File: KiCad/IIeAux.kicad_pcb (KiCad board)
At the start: 4 copper layers, 88.9 x 77.5 mm, 21 parts, among them J1 Apple IIe Aux, J4 PAL, U1 SN74LVC245AN, U2 TangNano9K, U3 74LS245, U4 74LS374, U5 SN74LVC245AN, U6 SN74LVC245AN, U7 SN74LVC245AN, U8 AE-LCNV4-MOSFET

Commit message: PCB V1.1
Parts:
- removed J4: PAL, IIeAux:PinHeader_1x02_P2.54mm_Horizontal
- removed R2: 0, IIeAux:R_Axial_DIN0207_L6.3mm_D2.5mm_P10.16mm_Horizontal
- removed the U8 at (109.9, 107.3)
- added C6: 0.1u, IIeAux:C_Disc_D4.3mm_W1.9mm_P5.08mm, F.Cu at (169.5, 111.8)
- added J2: Double Hi-Res, IIeAux:PinHeader_1x02_P2.54mm_Horizontal, F.Cu at (117.5, 131.4)
- added J3: PAL, IIeAux:PinHeader_1x02_P2.54mm_Horizontal, F.Cu at (118.1, 83.2)
- added U2: SN74LVC245AN, IIeAux:DIP-20_W7.62mm_Socket, F.Cu at (114.3, 105.4)
- J1: value Apple IIe Aux -> Aux Slot
- R1: value 4K7 -> R
- U3: renamed from U5; footprint IIeAux:DIP-20_W7.62mm -> IIeAux:DIP-20_W7.62mm_Socket
- U4: renamed from U6; footprint IIeAux:DIP-20_W7.62mm -> IIeAux:DIP-20_W7.62mm_Socket
- U5: renamed from U1; footprint IIeAux:DIP-20_W7.62mm -> IIeAux:DIP-20_W7.62mm_Socket
- U8: renamed from U7; footprint IIeAux:DIP-20_W7.62mm -> IIeAux:DIP-20_W7.62mm_Socket
- moved C7 62.7 mm to (169.5, 123.2)
- moved U7 46.7 mm to (172.7, 119.4)
- moved RN1 43.2 mm to (172.7, 108.6)
- moved C4 43.2 mm to (111.1, 111.8)
- moved U3 27.7 mm to (143.5, 105.4)
- moved U4 27.7 mm to (172.7, 105.4)
- moved C3 27.7 mm to (169.5, 97.8)
- moved C2 27.4 mm to (140.3, 97.8)
- moved U8 19.8 mm to (172.7, 130.8)
- moved C5 19.1 mm to (140.3, 111.8)
- moved C1 18.0 mm to (111.1, 97.8)
- moved U6 16.9 mm to (143.5, 119.4)
- moved U1 16.9 mm to (135.9, 94.6)
- moved D1 13.9 mm to (198.1, 71.8)
- moved U5 12.8 mm to (114.3, 119.4)
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- renumbered C5 to C2, C2 to C4, C6 to C5, C4 to C7, C7 to C8, U2 to U1, U4 to U6, U3 to U7
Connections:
- net Net-(U2-IOT10A_84) renamed A5
- net Net-(U2-IOT10B_83) renamed A4
- net Net-(U2-IOT11A_82) renamed A3
- net Net-(U2-IOT11B_81) renamed A2
- net Net-(U2-IOT12A_80) renamed A1
- net Net-(U2-IOT12B_79) renamed A0
- net Net-(U2-IOT8A_86) renamed A7
- net Net-(U2-IOT8B_85) renamed A6
- C2 pad 1: +5V -> +3V3
- U1 pad 1: Net-(U2-38_IOB31B) -> RA_EN
- U1 pad 10: Net-(U1-A6) -> Net-(U1-30_IOB13B)
- U1 pad 11: Net-(U1-A7) -> Net-(U1-33_IOB23A)
- U1 pad 12: Net-(U1-A8) -> Net-(U1-34_IOB23B)
- U1 pad 13: Net-(U2-40_IOB33B) -> Net-(U1-40_IOB33B)
- U1 pad 14: Net-(U2-35_IOB29A) -> Net-(U1-35_IOB29A)
- U1 pad 2: Net-(U2-37_IOB31A) -> VID_EN
- U1 pad 27: Net-(U2-IOB15B_32) -> Net-(U1-IOB15B_32)
- U1 pad 28: Net-(U2-IOB15A_31) -> Net-(U1-IOB15A_31)
- U1 pad 29: Net-(U2-IOR24A_49) -> Net-(U1-IOR24A_49)
- U1 pad 3: Net-(U2-36_IOB29B) -> D_R/W
- U1 pad 30: Net-(U2-IOR24B_48) -> Net-(U1-IOR24B_48)
- U1 pad 38: Net-(U2-IOT37B_76) -> Net-(U1-IOT37B_76)
- U1 pad 39: Net-(U2-IOT37A_77) -> Net-(U1-IOT37A_77)
- U1 pad 4: Net-(U2-39_IOB33A) -> MD_EN
- U1 pad 5: Net-(U1-A1) -> Net-(U1-25_IOB8A)
- U1 pad 6: Net-(U1-A2) -> Net-(U1-26_IOB8B)
- U1 pad 7: Net-(U1-A3) -> Net-(U1-27_IOB11A)
- U1 pad 8: Net-(U1-A4) -> Net-(U1-28_IOB11B)
- U1 pad 9: Net-(U1-A5) -> Net-(U1-29_IOB13A)
- U3 pad 19: GND -> VID_EN
- U3 pad 2: RA0 -> VID7
- U3 pad 3: RA1 -> VID6
- U3 pad 4: RA2 -> VID5
- U3 pad 5: RA3 -> VID4
- U3 pad 6: RA4 -> VID3
- U3 pad 7: RA5 -> VID2
- U3 pad 8: RA6 -> VID1
- U3 pad 9: RA7 -> VID0
- U4 pad 1: +3V3 -> D_R/W
- U4 pad 11: Net-(U2-35_IOB29A) -> Net-(U1-IOB15B_32)
- U4 pad 12: Net-(U2-40_IOB33B) -> Net-(U1-IOB15A_31)
- U4 pad 13: Net-(U2-IOB15B_32) -> Net-(U1-IOR24A_49)
- U4 pad 14: Net-(U2-IOB15A_31) -> Net-(U1-IOR24B_48)
- U4 pad 15: Net-(U2-IOR24A_49) -> Net-(U1-IOT37B_76)
- U4 pad 16: Net-(U2-IOR24B_48) -> Net-(U1-IOT37A_77)
- U4 pad 17: Net-(U2-IOT37B_76) -> Net-(U1-40_IOB33B)
- U4 pad 18: Net-(U2-IOT37A_77) -> Net-(U1-35_IOB29A)
- U4 pad 2: VID0 -> D0
- U4 pad 3: VID1 -> D1
- U4 pad 4: VID2 -> D2
- U4 pad 5: VID3 -> D3
- U4 pad 6: VID4 -> D4
- U4 pad 7: VID5 -> D5
- U4 pad 8: VID6 -> D6
- U4 pad 9: VID7 -> D7
- U5 pad 1: R/W80 -> +3V3
- U5 pad 11: D7 -> Net-(U1-34_IOB23B)
- U5 pad 12: D6 -> Net-(U1-33_IOB23A)
- U5 pad 13: D5 -> Net-(U1-30_IOB13B)
- U5 pad 14: D4 -> Net-(U1-29_IOB13A)
- U5 pad 15: D3 -> Net-(U1-28_IOB11B)
- U5 pad 16: D2 -> Net-(U1-27_IOB11A)
- U5 pad 17: D1 -> Net-(U1-26_IOB8B)
- U5 pad 18: D0 -> Net-(U1-25_IOB8A)
- U5 pad 2: Net-(U1-A1) -> GR
- U5 pad 3: Net-(U1-A2) -> RA10
- U5 pad 4: Net-(U1-A3) -> RA9
- U5 pad 5: Net-(U1-A4) -> Q3
- U5 pad 6: Net-(U1-A5) -> SYNC
- U5 pad 7: Net-(U1-A6) -> PRAS
- U5 pad 8: Net-(U1-A7) -> C07X
- U5 pad 9: Net-(U1-A8) -> R/W
- U6 pad 12: VID4 -> VID3
- U6 pad 13: D4 -> D3
- U6 pad 14: D5 -> D2
- U6 pad 15: VID5 -> VID2
- U6 pad 16: VID6 -> VID1
- U6 pad 17: D6 -> D1
- U6 pad 18: D7 -> D0
- U6 pad 19: VID7 -> VID0
- U6 pad 2: VID0 -> VID7
- U6 pad 3: D0 -> D7
- U6 pad 4: D1 -> D6
- U6 pad 5: VID1 -> VID6
- U6 pad 6: VID2 -> VID5
- U6 pad 7: D2 -> D5
- U6 pad 8: D3 -> D4
- U6 pad 9: VID3 -> VID4
- U7 pad 19: EN80 -> MD_EN
- U8 pad 2: PRAS -> PHI0
- U8 pad 3: Q3 -> PHI1
- U8 pad 4: R/W80 -> 80VID
- U8 pad 5: GR -> EN80
- U8 pad 6: 80VID -> R/W80
- U8 pad 7: AN3 -> LDPS
- U8 pad 8: SYNC -> 14M
- U8 pad 9: 14M -> AN3
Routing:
- net AN3: track 46.9 -> 229.5 mm, vias 1 -> 0
- net +5V: track 249.5 -> 153.7 mm, vias 0 -> 3
- net EN80: track 102.5 -> 11.4 mm, vias 2 -> 0
- net Net-(U1-41_IOB41A): track 7.92 -> 95.9 mm
- net D0: track 127.4 -> 43.8 mm, vias 2 -> 0
- net VID7: track 127.9 -> 44.7 mm, vias 1 -> 0
- net RA6: track 134.2 -> 52.3 mm, vias 1 -> 0
- net R/W80: track 93.7 -> 12.3 mm, vias 2 -> 0
- net D2: track 118.5 -> 37.4 mm, vias 2 -> 0
- net RA7: track 121.6 -> 41.7 mm, vias 2 -> 1
- net Net-(U1-42_IOB41B): track 7.92 -> 87.7 mm
- net D1: track 122.7 -> 43.8 mm, vias 2 -> 0
- net RA5: track 131.1 -> 55.2 mm, vias 0 -> 1
- net D3: track 112.5 -> 37.4 mm, vias 2 -> 0
- net +3V3: track 237.4 -> 309.9 mm
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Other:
- board size 88.9 x 77.5 mm -> 99.7 x 77.5 mm
- board text added: "IIeAux RGB Card"
- board text added: "V1.1 2026 nanja.info"
- board text removed: "2026 nanja.info"

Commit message: V1.0 first batch
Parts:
- removed the C6 at (169.5, 111.8)
- removed the U2 at (114.3, 105.4)
- added J4: PAL, IIeAux:PinHeader_1x02_P2.54mm_Horizontal, F.Cu at (118.1, 85.1)
- added J5: Y, IIeAux:PinSocket_1x08_P2.54mm_Vertical, B.Cu at (160.0, 117.5)
- added J6: X, IIeAux:PinSocket_1x08_P2.54mm_Vertical, B.Cu at (166.4, 76.2)
- J1: value Aux Slot -> Apple IIe Aux
- J2: value Double Hi-Res -> Double HiRes
- J3: value PAL -> Aux; footprint IIeAux:PinHeader_1x02_P2.54mm_Horizontal -> IIeAux:PinSocket_2x30_P2.54mm; moved to B.Cu
- R1: value R -> 4K7
- U1: renamed from U5; footprint IIeAux:DIP-20_W7.62mm_Socket -> IIeAux:DIP-20_W7.62mm
- U5: renamed from U3; footprint IIeAux:DIP-20_W7.62mm_Socket -> IIeAux:DIP-20_W7.62mm
- U6: renamed from U4; footprint IIeAux:DIP-20_W7.62mm_Socket -> IIeAux:DIP-20_W7.62mm
- U7: renamed from U8; footprint IIeAux:DIP-20_W7.62mm_Socket -> IIeAux:DIP-20_W7.62mm
- moved C2 73.1 mm to (184.2, 109.2)
- moved C4 58.5 mm to (131.4, 78.7), turned to 90 degrees
- moved J3 52.7 mm to (119.4, 135.9), turned to -90 degrees
- moved C5 50.0 mm to (184.2, 121.9)
- moved U3 46.8 mm to (127.0, 129.5)
- moved RN1 46.6 mm to (127.0, 117.5)
- moved D2 33.3 mm to (190.5, 104.1)
- moved C3 32.0 mm to (190.5, 73.7)
- moved U6 28.1 mm to (163.8, 78.7)
- moved U5 27.7 mm to (135.9, 78.7)
- moved U7 22.5 mm to (157.5, 114.3)
- moved C6 21.0 mm to (121.9, 121.9)
- moved C7 19.4 mm to (190.5, 120.7), turned to 0 degrees
- moved U4 17.3 mm to (157.5, 129.5)
- moved U2 16.9 mm to (121.9, 104.1)
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- renumbered C4 to C2, C7 to C4, C2 to C5, C5 to C6, C8 to C7, D1 to D2, U1 to U2, U7 to U3, U6 to U4
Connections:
- net A0 renamed Net-(U2-IOT12B_79)
- net A1 renamed Net-(U2-IOT12A_80)
- net A2 renamed Net-(U2-IOT11B_81)
- net A3 renamed Net-(U2-IOT11A_82)
- net A4 renamed Net-(U2-IOT10B_83)
- net A5 renamed Net-(U2-IOT10A_84)
- net A6 renamed Net-(U2-IOT8B_85)
- net A7 renamed Net-(U2-IOT8A_86)
- C5 pad 1: +3V3 -> +5V
- J3 pad 1: GND -> 3.58M
- J3 pad 2: Net-(J3-Pin_2) -> VID7M
- R1 pad 2: Net-(J3-Pin_2) -> Net-(J4-Pin_1)
- U1 pad 1: +3V3 -> R/W
- U1 pad 2: GR -> D0
- U1 pad 3: RA10 -> D1
- U1 pad 4: RA9 -> D2
- U1 pad 5: Q3 -> D3
- U1 pad 6: SYNC -> D4
- U1 pad 7: PRAS -> D5
- U1 pad 8: C07X -> D6
- U1 pad 9: R/W -> D7
- U2 pad 1: RA_EN -> unconnected-(U2-38_IOB31B-Pad1)
- U2 pad 13: Net-(U1-40_IOB33B) -> Net-(U2-40_IOB33B)
- U2 pad 14: Net-(U1-35_IOB29A) -> Net-(U2-35_IOB29A)
- U2 pad 2: VID_EN -> unconnected-(U2-37_IOB31A-Pad2)
- U2 pad 27: Net-(U1-IOB15B_32) -> Net-(U2-IOB15B_32)
- U2 pad 28: Net-(U1-IOB15A_31) -> Net-(U2-IOB15A_31)
- U2 pad 29: Net-(U1-IOR24A_49) -> Net-(U2-IOR24A_49)
- U2 pad 3: D_R/W -> unconnected-(U2-36_IOB29B-Pad3)
- U2 pad 30: Net-(U1-IOR24B_48) -> Net-(U2-IOR24B_48)
- U2 pad 38: Net-(U1-IOT37B_76) -> Net-(U2-IOT37B_76)
- U2 pad 39: Net-(U1-IOT37A_77) -> Net-(U2-IOT37A_77)
- U2 pad 4: MD_EN -> unconnected-(U2-39_IOB33A-Pad4)
- U2 pad 48: Net-(J3-Pin_2) -> Net-(J4-Pin_1)
- U3 pad 19: MD_EN -> EN80
- U4 pad 12: VID3 -> VID4
- U4 pad 13: D3 -> D4
- U4 pad 14: D2 -> D5
- U4 pad 15: VID2 -> VID5
- U4 pad 16: VID1 -> VID6
- U4 pad 17: D1 -> D6
- U4 pad 18: D0 -> D7
- U4 pad 19: VID0 -> VID7
- U4 pad 2: VID7 -> VID0
- U4 pad 3: D7 -> D0
- U4 pad 4: D6 -> D1
- U4 pad 5: VID6 -> VID1
- U4 pad 6: VID5 -> VID2
- U4 pad 7: D5 -> D2
- U4 pad 8: D4 -> D3
- U4 pad 9: VID4 -> VID3
- U5 pad 19: VID_EN -> GND
- U5 pad 2: VID7 -> RA0
- U5 pad 3: VID6 -> RA1
- U5 pad 4: VID5 -> RA2
- U5 pad 5: VID4 -> RA3
- U5 pad 6: VID3 -> RA4
- U5 pad 7: VID2 -> RA5
- U5 pad 8: VID1 -> RA6
- U5 pad 9: VID0 -> RA7
- U6 pad 1: D_R/W -> +3V3
- U6 pad 11: Net-(U1-IOB15B_32) -> Net-(U2-35_IOB29A)
- U6 pad 12: Net-(U1-IOB15A_31) -> Net-(U2-40_IOB33B)
- U6 pad 13: Net-(U1-IOR24A_49) -> Net-(U2-IOB15B_32)
- U6 pad 14: Net-(U1-IOR24B_48) -> Net-(U2-IOB15A_31)
- U6 pad 15: Net-(U1-IOT37B_76) -> Net-(U2-IOR24A_49)
- U6 pad 16: Net-(U1-IOT37A_77) -> Net-(U2-IOR24B_48)
- U6 pad 17: Net-(U1-40_IOB33B) -> Net-(U2-IOT37B_76)
- U6 pad 18: Net-(U1-35_IOB29A) -> Net-(U2-IOT37A_77)
- U6 pad 2: D0 -> X0
- U6 pad 3: D1 -> X1
- U6 pad 4: D2 -> X2
- U6 pad 5: D3 -> X3
- U6 pad 6: D4 -> X4
- U6 pad 7: D5 -> X5
- U6 pad 8: D6 -> X6
- U6 pad 9: D7 -> X7
- U7 pad 2: PHI0 -> Y0
- U7 pad 3: PHI1 -> Y1
- U7 pad 4: 80VID -> Y2
- U7 pad 5: EN80 -> Y3
- U7 pad 6: R/W80 -> Y4
- U7 pad 7: LDPS -> Y5
- U7 pad 8: 14M -> Y6
- U7 pad 9: AN3 -> Y7
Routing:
- net GND: track 5.08 -> 407.6 mm, vias 252 -> 4
- net AN3: track 229.5 -> 47.1 mm
- net +3V3: track 309.9 -> 231.1 mm
- net Net-(U2-41_IOB41A): track 95.9 -> 17.6 mm, vias 0 -> 1
- net Net-(U2-42_IOB41B): track 87.7 -> 16.3 mm, vias 0 -> 1
- net VID3: track 83.8 -> 14.8 mm, vias 1 -> 0
- net Net-(U2-51_IOR17B): track 79.6 -> 15.0 mm, vias 0 -> 1
- net EN80: track 11.4 -> 75.0 mm, vias 0 -> 1
- net RA7: track 41.7 -> 103.3 mm, vias 1 -> 2
- net Net-(U2-IOT12B_79): track 85.6 -> 25.2 mm, vias 1 -> 0
- net Net-(U2-53_IOR15B): track 71.4 -> 13.7 mm, vias 0 -> 1
- net Net-(U2-IOT12A_80): track 79.3 -> 25.2 mm, vias 1 -> 0
- net Net-(U2-40_IOB33B): track 0.00 -> 53.2 mm, vias 0 -> 1
- net Net-(U2-35_IOB29A): track 0.00 -> 51.6 mm, vias 0 -> 1
- net Net-(U2-54_IOR15A): track 63.3 -> 12.8 mm, vias 0 -> 1
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- removed copper zone on In1.Cu, net GND
- removed copper zone on In2.Cu, net GND
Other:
- board size 99.7 x 77.5 mm -> 88.9 x 77.5 mm
- copper layers 4 -> 2
- board text added: "+5V"
- board text added: "14M"
- board text added: "2025 nanja.info"
- board text added: "3.58M"
- board text added: "7M"
- board text added: "80VID"
- board text added: "ALTVID"
- board text added: "AN3"
- board text added: "C07X"
- board text added: "CASEN"
- board text added: "CLRGAT"
- board text added: "EN80"
- board text added: "ENTMG"
- board text added: "ENVID"
- board text added: "FRCTXT"
- board text added: "GND"
- board text added: "GR"
- board text added: "H0"
- board text added: "LDPS"
- board text added: "MD0"
- board text added: "MD1"
- board text added: "MD2"
- board text added: "MD3"
- board text added: "MD4"
- board text added: "MD5"
- board text added: "MD6"
- board text added: "MD7"
- board text added: "PCAS"
- board text added: "PHI0"
- board text added: "PHI1"
- board text added: "PRAS"
- board text added: "R/W"
- board text added: "R/W80"
- board text added: "RA0"
- board text added: "RA1"
- board text added: "RA10"
- board text added: "RA2"
- board text added: "RA3"
- board text added: "RA4"
- board text added: "RA5"
- board text added: "RA6"
- board text added: "RA7"
- board text added: "RA9"
- board text added: "ROMEN1"
- board text added: "ROMEN2"
- board text added: "SEGA"
- board text added: "SEGB"
- board text added: "SEROUT"
- board text added: "SYNC"
- board text added: "VC"
- board text added: "VID 7M"
- board text added: "VID0"
- board text added: "VID1"
- board text added: "VID2"
- board text added: "VID3"
- board text added: "VID4"
- board text added: "VID5"
- board text added: "VID6"
- board text added: "VID7"
- board text added: "WNDW"
- board text added: "X0"
- board text added: "X1"
- board text added: "X2"
- board text added: "X3"
- board text added: "X4"
- board text added: "X5"
- board text added: "X6"
- board text added: "X7"
- board text added: "Y0"
- board text added: "Y1"
- board text added: "Y2"
- board text added: "Y3"
- board text added: "Y4"
- board text added: "Y5"
- board text added: "Y6"
- board text added: "Y7"
- board text removed: "IIeAux RGB Card"
- board text removed: "V1.1 2026 nanja.info"

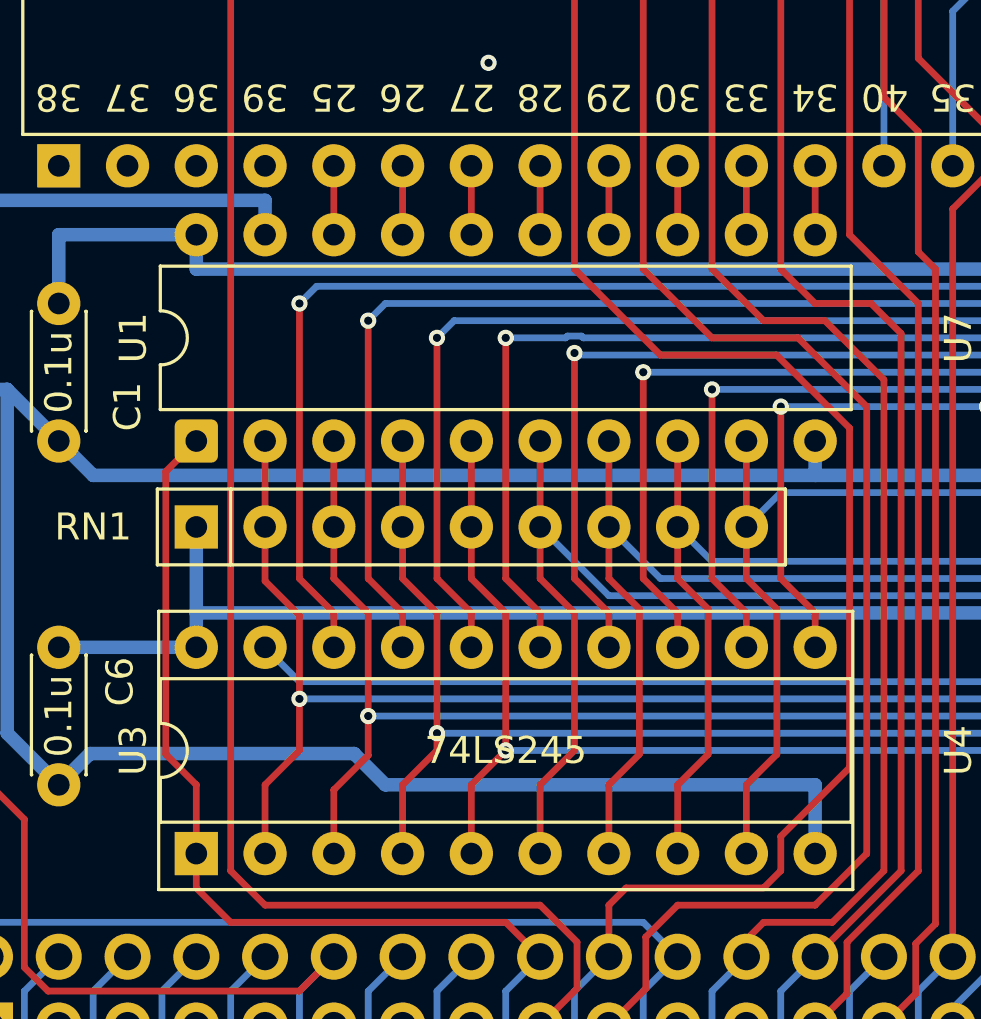
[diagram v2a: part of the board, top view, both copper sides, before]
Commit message: fixed U1 direction
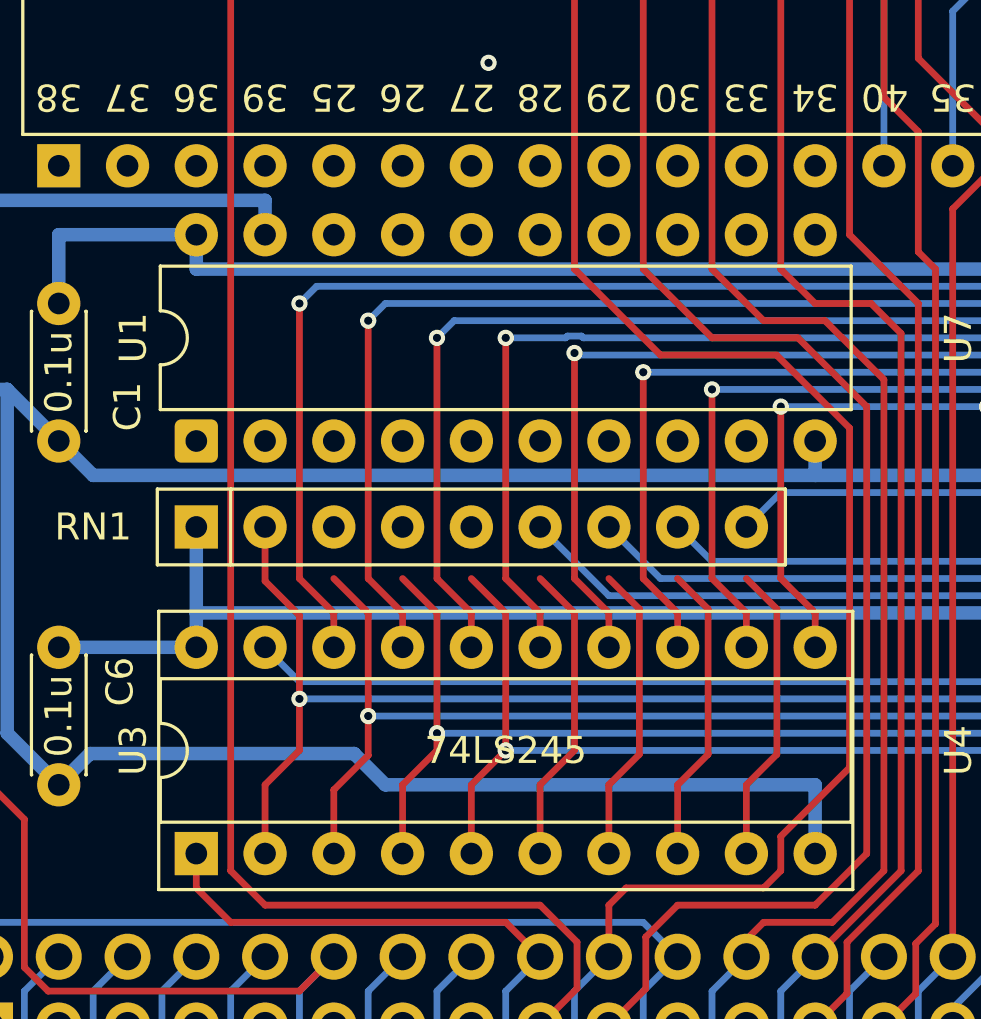
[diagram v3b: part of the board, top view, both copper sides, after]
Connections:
- U1 pad 1: R/W -> R/W80
- U1 pad 11: Net-(U1-B8) -> D7
- U1 pad 12: Net-(U1-B7) -> D6
- U1 pad 13: Net-(U1-B6) -> D5
- U1 pad 14: Net-(U1-B5) -> D4
- U1 pad 15: Net-(U1-B4) -> D3
- U1 pad 16: Net-(U1-B3) -> D2
- U1 pad 17: Net-(U1-B2) -> D1
- U1 pad 18: Net-(U1-B1) -> D0
- U1 pad 2: D0 -> Net-(U1-A1)
- U1 pad 3: D1 -> Net-(U1-A2)
- U1 pad 4: D2 -> Net-(U1-A3)
- U1 pad 5: D3 -> Net-(U1-A4)
- U1 pad 6: D4 -> Net-(U1-A5)
- U1 pad 7: D5 -> Net-(U1-A6)
- U1 pad 8: D6 -> Net-(U1-A7)
- U1 pad 9: D7 -> Net-(U1-A8)
- U2 pad 10: Net-(U1-B6) -> Net-(U1-A6)
- U2 pad 11: Net-(U1-B7) -> Net-(U1-A7)
- U2 pad 12: Net-(U1-B8) -> Net-(U1-A8)
- U2 pad 5: Net-(U1-B1) -> Net-(U1-A1)
- U2 pad 6: Net-(U1-B2) -> Net-(U1-A2)
- U2 pad 7: Net-(U1-B3) -> Net-(U1-A3)
- U2 pad 8: Net-(U1-B4) -> Net-(U1-A4)
- U2 pad 9: Net-(U1-B5) -> Net-(U1-A5)
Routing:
- net R/W: track 41.1 -> 25.0 mm
- net D7: track 39.1 -> 34.0 mm
- net D6: track 43.5 -> 38.5 mm
- net D5: track 50.0 -> 44.9 mm
- net D4: track 55.7 -> 50.6 mm
- net D3: track 56.9 -> 51.9 mm
- net D2: track 57.6 -> 52.5 mm
- net D1: track 53.1 -> 48.0 mm
- net D0: track 53.8 -> 50.6 mm
- net Net-(U1-B8): track 2.55 -> 0.00 mm
- net Net-(U1-B7): track 2.55 -> 0.00 mm
- net Net-(U1-B6): track 2.55 -> 0.00 mm
- net Net-(U1-B5): track 2.55 -> 0.00 mm
- net Net-(U1-B4): track 2.55 -> 0.00 mm
- net Net-(U1-B3): track 2.55 -> 0.00 mm
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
